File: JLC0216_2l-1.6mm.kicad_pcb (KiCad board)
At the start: 4 copper layers, 24 x 24 mm, 0 parts

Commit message: update stack
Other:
- copper layers 4 -> 2
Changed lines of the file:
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@@
 	(generator_version "8.0")
 	(general
-		(thickness 1.5742)
+		(thickness 1.555)
 		(legacy_teardrops no)
 	)
@@
 		(date "SET!!!")
 		(rev "VERV")
-		(company "ELT")
+		(company "SET!!!")
 		(comment 2 "SET!!!")
 		(comment 3 "SET!!!")
@@
 	(layers
 		(0 "F.Cu" signal)
-		(1 "In1.Cu" power)
-		(2 "In2.Cu" power)
 		(31 "B.Cu" signal)
 		(32 "B.Adhes" user "B.Adhesive")
@@
 			(layer "F.Mask"
 				(type "Top Solder Mask")
-				(thickness 0.005)
+				(thickness 0.01)
 			)
 			(layer "F.Cu"
@@
 			)
 			(layer "dielectric 1"
-				(type "prepreg")
-				(thickness 0.0994)
-				(material "3313")
-				(epsilon_r 4.1)
-				(loss_tangent 0.002)
-			)
-			(layer "In1.Cu"
-				(type "copper")
-				(thickness 0.0152)
-			)
-			(layer "dielectric 2"
 				(type "core")
 				(color "FR4 natural")
-				(thickness 1.265)
+				(thickness 1.465)
 				(material "FR4")
 				(epsilon_r 4.5)
 				(loss_tangent 0.02)
 			)
-			(layer "In2.Cu"
-				(type "copper")
-				(thickness 0.0152)
-			)
-			(layer "dielectric 3"
-				(type "prepreg")
-				(color "FR4 natural")
-				(thickness 0.0994)
-				(material "3313")
-				(epsilon_r 4.1)
-				(loss_tangent 0.002)
-			)
 			(layer "B.Cu"
 				(type "copper")
@@
 			(layer "B.Mask"
 				(type "Bottom Solder Mask")
-				(thickness 0.005)
+				(thickness 0.01)
 			)
 			(layer "B.Paste"
@@
 			)
 			(copper_finish "HAL SnPb")
-			(dielectric_constraints no)
+			(dielectric_constraints yes)
 		)
 		(pad_to_mask_clearance 0)
@@
 		(layer "Dwgs.User")
 	)
+	(gr_line
+		(start 34 30)
+		(end 50 30)
+		(stroke
+			(width 0.1)
+			(type default)
+		)
+		(layer "Edge.Cuts")
+	)
+	(gr_arc
+		(start 54 50)
+		(mid 52.828427 52.828427)
+		(end 49.999999 54.000001)
+		(stroke
+			(width 0.1)
+			(type default)
+		)
+		(layer "Edge.Cuts")
+	)
+	(gr_line
+		(start 49.999999 54.000001)
+		(end 33.999999 54.000001)
+		(stroke
+			(width 0.1)
+			(type default)
+		)
+		(layer "Edge.Cuts")
+	)
+	(gr_arc
+		(start 29.999999 34.000001)
+		(mid 31.171572 31.171573)
+		(end 34 30)
+		(stroke
+			(width 0.1)
+			(type default)
+		)
+		(layer "Edge.Cuts")
+	)
+	(gr_arc
+		(start 50 30)
+		(mid 52.828428 31.171573)
+		(end 54.000001 34.000001)
+		(stroke
+			(width 0.1)
+			(type default)
+		)
+		(layer "Edge.Cuts")
+	)
+	(gr_line
+		(start 29.999999 34.000001)
+		(end 29.999999 50)
+		(stroke
+			(width 0.1)
+			(type default)
+		)
+		(layer "Edge.Cuts")
+	)
 	(gr_arc
 		(start 34.000001 54.000001)
@@
 		(layer "Edge.Cuts")
 	)
-	(gr_arc
-		(start 50 30)
-		(mid 52.828428 31.171573)
-		(end 54.000001 34.000001)
-		(stroke
-			(width 0.1)
-			(type default)
-		)
-		(layer "Edge.Cuts")
-	)
-	(gr_line
-		(start 34 30)
-		(end 50 30)
-		(stroke
-			(width 0.1)
-			(type default)
-		)
-		(layer "Edge.Cuts")
-	)
-	(gr_arc
-		(start 54 50)
-		(mid 52.828427 52.828428)
-		(end 49.999999 54.000001)
-		(stroke
-			(width 0.1)
-			(type default)
-		)
-		(layer "Edge.Cuts")
-	)
 	(gr_line
 		(start 54 49.999999)
@@
 		(stroke
 			(width 0.1)
-			(type default)
-		)
-		(layer "Edge.Cuts")
-	)
-	(gr_line
-		(start 49.999999 54.000001)
-		(end 33.999999 54.000001)
-		(stroke
-			(width 0.1)
-			(type default)
-		)
-		(layer "Edge.Cuts")
-	)
-	(gr_arc
-		(start 29.999999 34.000001)
-		(mid 31.171572 31.171573)
-		(end 34 30)
-		(stroke
-			(width 0.1)
-			(type default)
-		)
-		(layer "Edge.Cuts")
-	)
-	(gr_line
-		(start 29.999999 34.000001)
-		(end 29.999999 50)
-		(stroke
-			(width 0.1)

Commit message: add default zone
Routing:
- added copper zone on F.Cu, net (none)
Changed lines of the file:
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@@
 		(layer "Edge.Cuts")
 	)
+	(zone
+		(net 0)
+		(net_name "")
+		(layer "F.Cu")
+		(hatch edge 0.5)
+		(connect_pads
+			(clearance 0.2)
+		)
+		(min_thickness 0.2)
+		(filled_areas_thickness no)
+		(fill
+			(thermal_gap 0.2)
+			(thermal_bridge_width 0.5)
+			(smoothing fillet)
+			(radius 1)
+			(island_removal_mode 1)
+			(island_area_min 10)
+		)
+		(polygon
+			(pts
+				(xy 29 29) (xy 55 29) (xy 55 55) (xy 29 55)
+			)
+		)
+	)
 )

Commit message: update silk
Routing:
- added copper zone on B.Cu, net (none)
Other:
- board text added: "JLCJLCJLCJLC"
- board text added: "TES"
- board text added: "VERV"
- board text added: "test test test"
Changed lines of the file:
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@@
 	(net 0 "")
+	(gr_line
+		(start 47.749999 37.874999)
+		(end 45.500001 37.874998)
+		(stroke
+			(width 0.1)
+			(type default)
+		)
+		(layer "F.SilkS")
+	)
+	(gr_line
+		(start 47.749999 37.874999)
+		(end 47.75 35.625)
+		(stroke
+			(width 0.1)
+			(type default)
+		)
+		(layer "F.SilkS")
+	)
+	(gr_line
+		(start 45.5 35.624999)
+		(end 45.500001 37.874998)
+		(stroke
+			(width 0.1)
+			(type default)
+		)
+		(layer "F.SilkS")
+	)
+	(gr_line
+		(start 47.75 35.625)
+		(end 45.5 35.624999)
+		(stroke
+			(width 0.1)
+			(type default)
+		)
+		(layer "F.SilkS")
+	)
+	(gr_rect
+		(start 36.5 39)
+		(end 41.5 44)
+		(stroke
+			(width 0.1)
+			(type solid)
+		)
+		(fill solid)
+		(layer "F.SilkS")
+	)
 	(gr_line
 		(start 30 31)
@@
 		(layer "Edge.Cuts")
 	)
+	(gr_text "TES"
+		(at 36.5 36.25 0)
+		(layer "F.SilkS")
+		(effects
+			(font
+				(size 1 1)
+				(thickness 0.2)
+				(bold yes)
+				(italic yes)
+			)
+			(justify left)
+		)
+	)
+	(gr_text "JLCJLCJLCJLC"
+		(at 41.5 46 0)
+		(layer "F.SilkS")
+		(effects
+			(font
+				(size 0.8 0.8)
+				(thickness 0.15)
+			)
+		)
+	)
+	(gr_text "VERV"
+		(at 44.75 36.374999 0)
+		(layer "F.SilkS")
+		(effects
+			(font
+				(size 0.8 0.8)
+				(thickness 0.15)
+				(bold yes)
+				(italic yes)
+			)
+			(justify right)
+		)
+	)
+	(gr_text "test test test"
+		(at 36.5 37.499999 0)
+		(layer "F.SilkS")
+		(effects
+			(font
+				(size 0.8 0.8)
+				(thickness 0.15)
+				(bold yes)
+			)
+			(justify left)
+		)
+	)
+	(dimension
+		(type aligned)
+		(layer "Dwgs.User")
+		(pts
+			(xy 49.999999 54.000001) (xy 50 30)
+		)
+		(height 7.999999)
+		(gr_text "24,0000 mm"
+			(at 56.849999 42 89.99999523)
+			(layer "Dwgs.User")
+			(effects
+				(font
+					(size 1 1)
+					(thickness 0.15)
+				)
+			)
+		)
+		(format
+			(prefix "")
+			(suffix "")
+			(units 3)
+			(units_format 1)
+			(precision 4)
+		)
+		(style
+			(thickness 0.1)
+			(arrow_length 1.27)
+			(text_position_mode 0)
+			(extension_height 0.58642)
+			(extension_offset 0.5) keep_text_aligned)
+	)
+	(dimension
+		(type aligned)
+		(layer "Dwgs.User")
+		(pts
+			(xy 30 50) (xy 54 50)
+		)
+		(height 7.999999)
+		(gr_text "24,0000 mm"
+			(at 42 56.849999 0)
+			(layer "Dwgs.User")
+			(effects
+				(font
+					(size 1 1)
+					(thickness 0.15)
+				)
+			)
+		)
+		(format
+			(prefix "")
+			(suffix "")
+			(units 3)
+			(units_format 1)
+			(precision 4)
+		)
+		(style
+			(thickness 0.1)
+			(arrow_length 1.27)
+			(text_position_mode 0)
+			(extension_height 0.58642)
+			(extension_offset 0.5) keep_text_aligned)
+	)
 	(zone
 		(net 0)
 		(net_name "")
-		(layer "F.Cu")
+		(layers "F&B.Cu")
 		(hatch edge 0.5)
 		(connect_pads
@@
 		)
 	)
+	(group ""
+		(members "fa853e0c-3ed8-4f2e-829c-ad59f6fd44db")
+	)
+	(group ""
+		(members "7bdefbd0-6765-4b4d-aaa2-1998c29d58b4" "a332cbd3-1ec2-49ef-beef-555777c9bb45"
+			"cd7aeb34-2f03-4657-8cd1-aa30d4322394"
+		)
+	)
+	(group ""
+		(members "0b17f976-a3b7-420e-9dd8-b1f7df76da22" "40fdecbb-083d-4882-a1c3-4dc0446a7ff9"
+			"8a25a8e2-c01c-4215-a8b7-29817698f92f" "8a5e4228-fa8f-4e79-a9a9-34edba54ab6e"
+		)
+	)

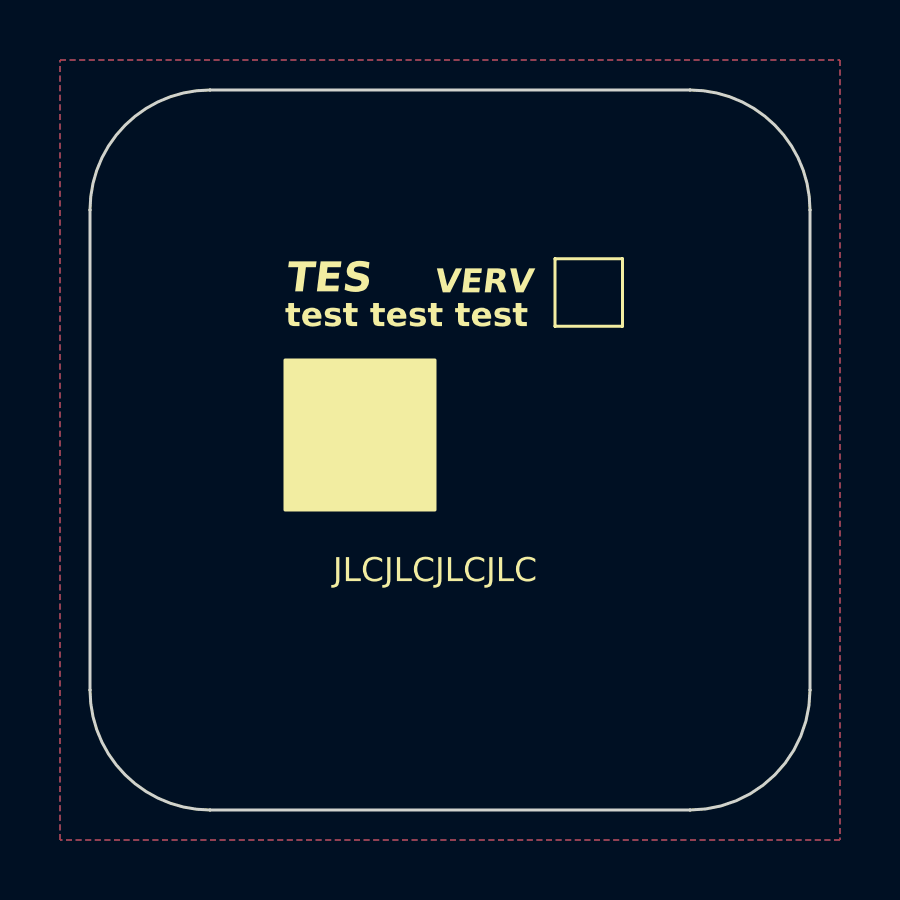
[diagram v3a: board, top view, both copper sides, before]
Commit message: Update to kicad9
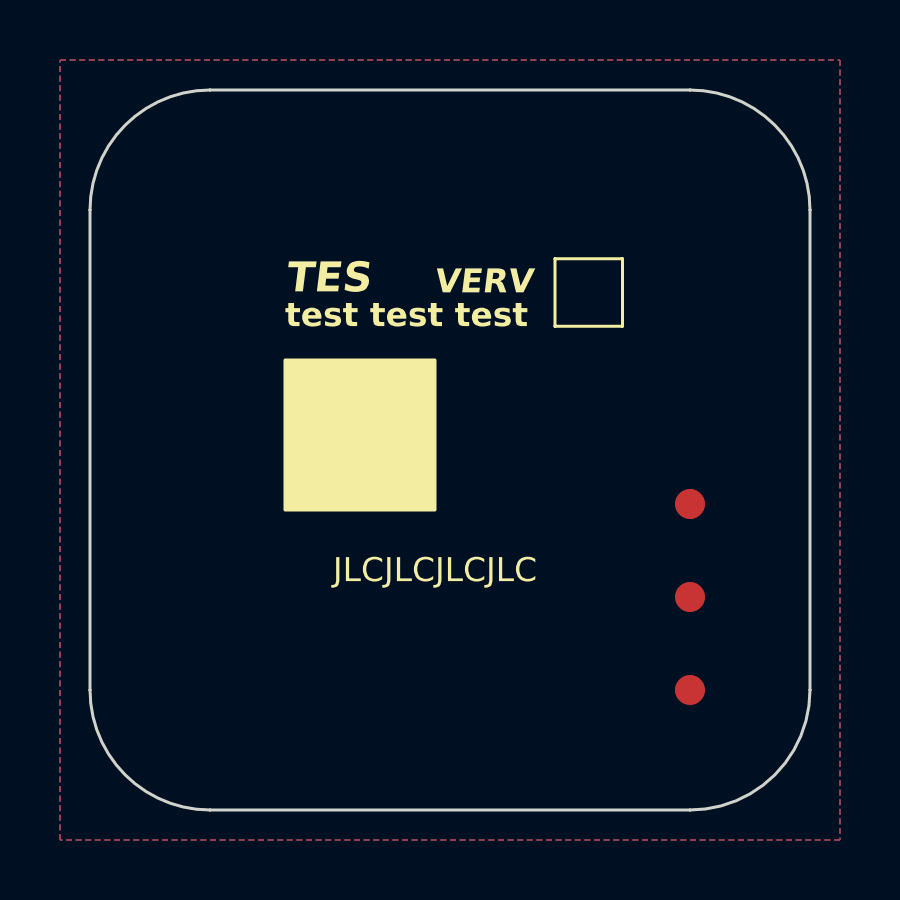
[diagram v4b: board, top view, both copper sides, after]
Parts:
- added FID1: Fiducial, MAS_Package_std:Fiducial_1mm_Mask2mm, F.Cu at (50.0, 43.8)
- added FID2: Fiducial, MAS_Package_std:Fiducial_1mm_Mask2mm, F.Cu at (50.0, 46.9)
- added FID3: Fiducial, MAS_Package_std:Fiducial_1mm_Mask2mm, F.Cu at (50.0, 50.0)
